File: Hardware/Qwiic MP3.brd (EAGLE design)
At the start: 25.4 x 50.8 mm, 97 parts, among them J1 MICRO-SD, J3 PTH, J7 ISP, J8 3.5mm Audio, J9 Poke-Home, U1 TPA2005D1, U2 WT2003S, U3 AP2112-3.3V, U4 ATTINY84-ARDUINO

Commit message: Nearing production code
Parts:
- C3, C6: value 10uF -> 0.22uF
- moved FRAME1 66.0 mm to (45.7, -17.8), flipped to the bottom
- moved J8 25.4 mm to (25.4, 39.4), flipped to the bottom
- moved U$20 24.6 mm to (25.0, 25.4), flipped to the bottom
- moved JP1 23.9 mm to (24.6, 50.0), flipped to the top
- moved JP6 23.9 mm to (24.6, 50.0), flipped to the bottom
- moved JP2 23.6 mm to (0.89, 0.89), flipped to the bottom
- moved JP5 23.6 mm to (0.89, 0.89), flipped to the top
- moved C5 20.3 mm to (2.54, 31.8), flipped to the bottom
- moved C7 20.3 mm to (2.54, 35.6), flipped to the bottom
- moved C8 20.3 mm to (2.54, 39.4), flipped to the bottom
- moved D1 20.3 mm to (2.54, 26.7), flipped to the bottom
- moved J6 20.3 mm to (22.9, 10.2), flipped to the bottom
- moved JP11 20.3 mm to (22.9, 2.54), flipped to the bottom
- moved JP13 20.3 mm to (2.54, 2.54), flipped to the bottom
- moved JP3 20.3 mm to (22.9, 48.3), flipped to the bottom
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
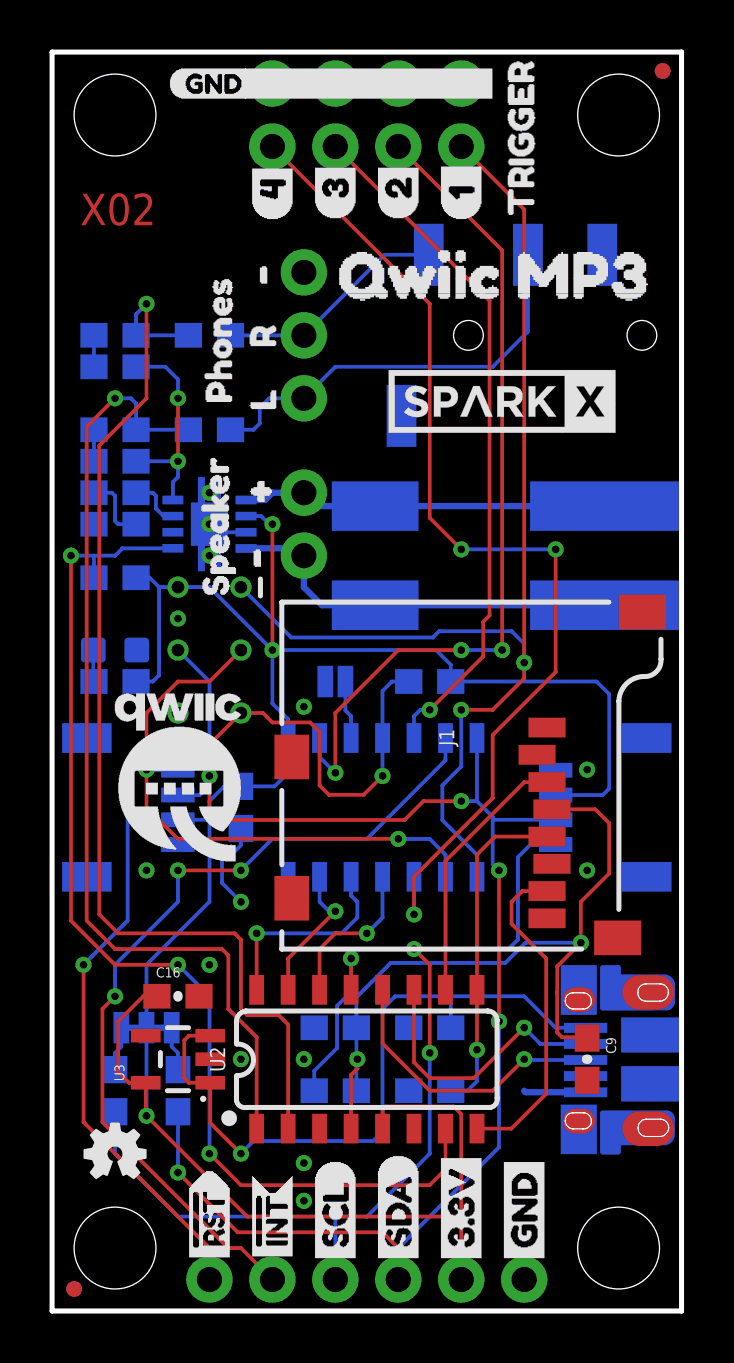
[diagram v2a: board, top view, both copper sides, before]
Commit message: Update to USB C
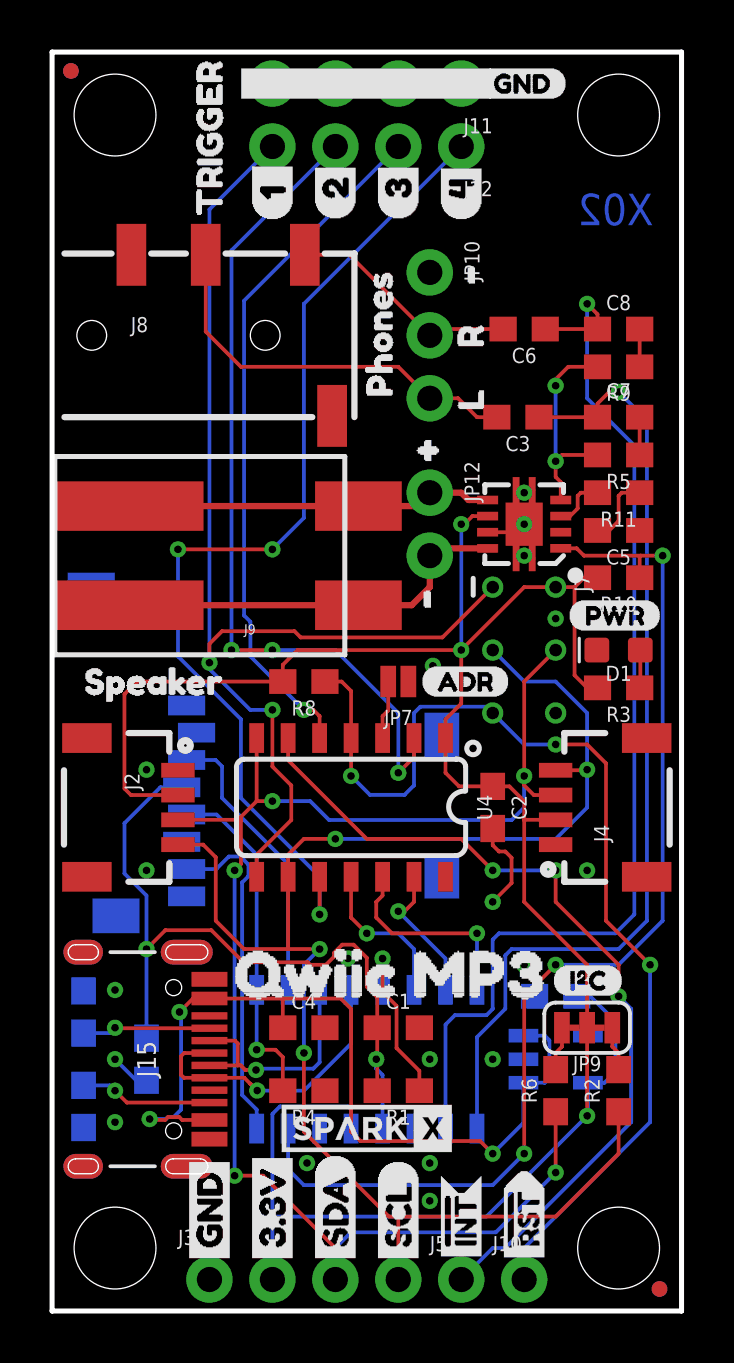
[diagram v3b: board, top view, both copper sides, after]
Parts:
- removed J6: (no value), SparkFun-Connectors:USB-MICROB-PTH-MILL
- added J15: (no value), SparkFun-Connectors:USB-C-16P
- added R13, R14: 5.1k, SparkFun-Resistors:0603
- C16, C9: device SparkFun-Capacitors:0603-CAP -> SparkFun-Capacitors:0603
- moved FRAME1 66.0 mm to (-20.3, -17.8), flipped to the top
- moved J8 25.4 mm to (0.00, 39.4), flipped to the top
- moved U$20 24.6 mm to (0.38, 25.4), flipped to the top
- moved JP1 23.9 mm to (0.76, 50.0), flipped to the bottom
- moved JP6 23.9 mm to (0.76, 50.0), flipped to the top
- moved JP2 23.6 mm to (24.5, 0.89), flipped to the top
- moved JP5 23.6 mm to (24.5, 0.89), flipped to the bottom
- moved C7 20.3 mm to (22.9, 36.1), flipped to the top
- moved C5 20.3 mm to (22.9, 31.5), flipped to the top
- moved C8 20.3 mm to (22.9, 39.6), flipped to the top
- moved R3 20.3 mm to (22.9, 25.1), flipped to the top
- moved R5 20.3 mm to (22.9, 34.5), flipped to the top
- moved D1 20.3 mm to (22.9, 26.7), flipped to the top
- moved JP11 20.3 mm to (2.54, 2.54), flipped to the top
- moved JP13 20.3 mm to (22.9, 2.54), flipped to the top
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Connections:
- new net N$1: J15.B5, R13.2
- new net N$2: J15.A5, R14.2
- net 5V: now also J15.VBUS1, J15.VBUS2; no longer J6.VBUS
- net D+: now also J15.A6, J15.B6; no longer J6.D+
- net D-: now also J15.A7, J15.B7; no longer J6.D-
- net GND: now also J15.GND, J15.GND2, J15.SHLD1, J15.SHLD2, J15.SHLD3, J15.SHLD4, J15.SHLD5, J15.SHLD6, J15.SHLD7, J15.SHLD8, R13.1, R14.1; no longer J6.GND, J6.SHIELD, J6.SHIELD10, J6.SHIELD2, J6.SHIELD3, J6.SHIELD4, J6.SHIELD5, J6.SHIELD6, J6.SHIELD7, J6.SHIELD8, J6.SHIELD9
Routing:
- net 5V: track 28.4 -> 34.6 mm, vias 1 -> 3
- net N$1: track 0.00 -> 5.37 mm, vias 0 -> 1
- net N$2: track 0.00 -> 5.18 mm, vias 0 -> 1
- net D-: track 11.2 -> 9.65 mm
- net SD_CMD: track 10.6 -> 11.7 mm
- net VCCIO: track 29.8 -> 30.9 mm
- net SCL: track 63.6 -> 62.6 mm
- net GND: track 9.35 -> 8.47 mm, vias 14 -> 19
- net AC-L: track 17.1 -> 16.3 mm
- net SDA: track 60.3 -> 61.0 mm
- net !RST: track 42.4 -> 43.0 mm
- net SD_DAT: track 13.3 -> 13.8 mm
